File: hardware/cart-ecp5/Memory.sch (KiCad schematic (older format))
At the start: 7 parts, among them J2 MicroSD_Molex_1040310811

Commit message: First pass annotation and footprint assignment complete
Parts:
- gave numbers to parts that had none: 1
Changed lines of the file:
@@
 $EndDescr
 $Comp
-L ng_memory:S27KS0641 U?
+L ng_memory:S27KS0641 U3
 U 1 1 5F47DAAE
 P 3600 4100
-F 0 "U?" H 3900 4900 60  0000 C CNN
+F 0 "U3" H 3900 4900 60  0000 C CNN
 F 1 "S27KS0641" H 4100 4800 60  0000 C CNN
 F 2 "ng_package_bga:BGA-24_6.0x8.0mm_Layout5x5_P1.0mm_Pad0.4mm" H 2800 6050 60  0001 C CNN
@@
 Connection ~ 3500 4850
 $Comp
-L ng_power:GND #PWR?
+L ng_power:GND #PWR09
 U 1 1 5F3CB04C
 P 3500 4950
-F 0 "#PWR?" H 3500 4700 50  0001 C CNN
+F 0 "#PWR09" H 3500 4700 50  0001 C CNN
 F 1 "GND" H 3503 4824 50  0000 C CNN
 F 2 "" H 3400 4600 50  0001 C CNN
@@
 AR Path="/5F8FA3AC" Ref="#PWR?"  Part="1"
 AR Path="/5F8F01DB/5F8FA3AC" Ref="#PWR018"  Part="1"
-AR Path="/5F7B735C/5F8FA3AC" Ref="#PWR?"  Part="1"
-F 0 "#PWR?" H 8400 4650 50  0001 C CNN
+AR Path="/5F7B735C/5F8FA3AC" Ref="#PWR012"  Part="1"
+F 0 "#PWR012" H 8400 4650 50  0001 C CNN
 F 1 "GND" H 8403 4774 50  0000 C CNN
 F 2 "" H 8300 4550 50  0001 C CNN
@@
 AR Path="/5F8FA3B4" Ref="J?"  Part="1"
 AR Path="/5F8F01DB/5F8FA3B4" Ref="J2"  Part="1"
-AR Path="/5F7B735C/5F8FA3B4" Ref="J?"  Part="1"
-F 0 "J?" H 8650 4600 50  0000 L CNN
+AR Path="/5F7B735C/5F8FA3B4" Ref="J2"  Part="1"
+F 0 "J2" H 8650 4600 50  0000 L CNN
 F 1 "MicroSD_Molex_1040310811" H 8650 4500 50  0000 L CNN
 F 2 "ng_conn:MicroSD_Molex_1040310811" H 8700 4000 50  0001 C CNN
@@
 AR Path="/5F8FA3CB" Ref="R?"  Part="1"
 AR Path="/5F8F01DB/5F8FA3CB" Ref="R1"  Part="1"
-AR Path="/5F7B735C/5F8FA3CB" Ref="R?"  Part="1"
-F 0 "R?" V 7700 3300 50  0000 L CNN
+AR Path="/5F7B735C/5F8FA3CB" Ref="R5"  Part="1"
+F 0 "R5" V 7700 3300 50  0000 L CNN
 F 1 "10k" V 7700 3000 50  0000 R CNN
 F 2 "Resistor_SMD:R_0603_1608Metric" V 7580 3150 50  0001 C CNN
@@
 AR Path="/5F8FA3D7" Ref="RN?"  Part="1"
 AR Path="/5F8F01DB/5F8FA3D7" Ref="RN3"  Part="1"
-AR Path="/5F7B735C/5F8FA3D7" Ref="RN?"  Part="1"
-F 0 "RN?" H 8188 3196 50  0000 L CNN
+AR Path="/5F7B735C/5F8FA3D7" Ref="RN1"  Part="1"
+F 0 "RN1" H 8188 3196 50  0000 L CNN
 F 1 "10k" H 8188 3105 50  0000 L CNN
 F 2 "Resistor_SMD:R_Array_Convex_4x0603" V 8275 3150 50  0001 C CNN
@@
 AR Path="/5F8FA3E3" Ref="C?"  Part="1"
 AR Path="/5F8F01DB/5F8FA3E3" Ref="C16"  Part="1"
-AR Path="/5F7B735C/5F8FA3E3" Ref="C?"  Part="1"
-F 0 "C?" H 6850 3150 50  0000 R CNN
+AR Path="/5F7B735C/5F8FA3E3" Ref="C3"  Part="1"
+F 0 "C3" H 6850 3150 50  0000 R CNN
 F 1 "10u" H 6850 2950 50  0000 R CNN
 F 2 "Capacitor_SMD:C_0805_2012Metric" H 6938 2900 50  0001 C CNN
@@
 AR Path="/5F8FA3E9" Ref="C?"  Part="1"
 AR Path="/5F8F01DB/5F8FA3E9" Ref="C17"  Part="1"
-AR Path="/5F7B735C/5F8FA3E9" Ref="C?"  Part="1"
-F 0 "C?" H 7150 3150 50  0000 R CNN
+AR Path="/5F7B735C/5F8FA3E9" Ref="C4"  Part="1"
+F 0 "C4" H 7150 3150 50  0000 R CNN
 F 1 "100n" H 7150 2950 50  0000 R CNN
 F 2 "Capacitor_SMD:C_0603_1608Metric" H 7238 2900 50  0001 C CNN
@@
 AR Path="/5F8FA3EF" Ref="#PWR?"  Part="1"
 AR Path="/5F8F01DB/5F8FA3EF" Ref="#PWR016"  Part="1"
-AR Path="/5F7B735C/5F8FA3EF" Ref="#PWR?"  Part="1"
-F 0 "#PWR?" H 6900 3050 50  0001 C CNN
+AR Path="/5F7B735C/5F8FA3EF" Ref="#PWR010"  Part="1"
+F 0 "#PWR010" H 6900 3050 50  0001 C CNN
 F 1 "GND" H 6903 3174 50  0000 C CNN
 F 2 "" H 6800 2950 50  0001 C CNN
@@
 AR Path="/5F8FA3F5" Ref="#PWR?"  Part="1"
 AR Path="/5F8F01DB/5F8FA3F5" Ref="#PWR017"  Part="1"
-AR Path="/5F7B735C/5F8FA3F5" Ref="#PWR?"  Part="1"
-F 0 "#PWR?" H 7200 3050 50  0001 C CNN
+AR Path="/5F7B735C/5F8FA3F5" Ref="#PWR011"  Part="1"
+F 0 "#PWR011" H 7200 3050 50  0001 C CNN
 F 1 "GND" H 7203 3174 50  0000 C CNN
 F 2 "" H 7100 2950 50  0001 C CNN
@@
 AR Path="/5EFEABF6" Ref="R?"  Part="1"
 AR Path="/5F8F01DB/5EFEABF6" Ref="R8"  Part="1"
-AR Path="/5F7B735C/5EFEABF6" Ref="R?"  Part="1"
-F 0 "R?" V 7600 3300 50  0000 L CNN
+AR Path="/5F7B735C/5EFEABF6" Ref="R4"  Part="1"
+F 0 "R4" V 7600 3300 50  0000 L CNN
 F 1 "10k" V 7600 3000 50  0000 R CNN
 F 2 "Resistor_SMD:R_0603_1608Metric" V 7480 3150 50  0001 C CNN

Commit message: Initial placement pass
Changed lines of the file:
@@
 AR Path="/5F8FA3D7" Ref="RN?"  Part="1"
 AR Path="/5F8F01DB/5F8FA3D7" Ref="RN3"  Part="1"
-AR Path="/5F7B735C/5F8FA3D7" Ref="RN1"  Part="1"
-F 0 "RN1" H 8188 3196 50  0000 L CNN
+AR Path="/5F7B735C/5F8FA3D7" Ref="RN7"  Part="1"
+F 0 "RN7" H 8188 3196 50  0000 L CNN
 F 1 "10k" H 8188 3105 50  0000 L CNN
 F 2 "Resistor_SMD:R_Array_Convex_4x0603" V 8275 3150 50  0001 C CNN

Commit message: Shrink smallest passive to 0402
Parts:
- C16: footprint Capacitor_SMD:C_0805_2012Metric -> Capacitor_SMD:C_0603_1608Metric; MPN CL21A106KAYNNNE -> (none); Place DNP -> (none)
- C17: footprint Capacitor_SMD:C_0603_1608Metric -> Capacitor_SMD:C_0402_1005Metric; MPN CL10B104KB8NNNC -> (none)
- R1, R8: footprint Resistor_SMD:R_0603_1608Metric -> Resistor_SMD:R_0402_1005Metric; MPN RC0603FR-0710KL -> (none)
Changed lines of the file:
@@
 F 0 "R5" V 7700 3300 50  0000 L CNN
 F 1 "10k" V 7700 3000 50  0000 R CNN
-F 2 "Resistor_SMD:R_0603_1608Metric" V 7580 3150 50  0001 C CNN
+F 2 "Resistor_SMD:R_0402_1005Metric" V 7580 3150 50  0001 C CNN
 F 3 "~" H 7650 3150 50  0001 C CNN
-F 4 "RC0603FR-0710KL" H 7650 3150 50  0001 C CNN "MPN"
+F 4 "" H 7650 3150 50  0001 C CNN "MPN"
 	1    7650 3150
 	1    0    0    -1
@@
 F 0 "C3" H 6850 3150 50  0000 R CNN
 F 1 "10u" H 6850 2950 50  0000 R CNN
-F 2 "Capacitor_SMD:C_0805_2012Metric" H 6938 2900 50  0001 C CNN
+F 2 "Capacitor_SMD:C_0603_1608Metric" H 6938 2900 50  0001 C CNN
 F 3 "~" H 6900 3050 50  0001 C CNN
-F 4 "CL21A106KAYNNNE" H 6900 3050 50  0001 C CNN "MPN"
-F 5 "DNP" H 6850 2850 50  0000 R CNN "Place"
+F 4 "" H 6900 3050 50  0001 C CNN "MPN"
 	1    6900 3050
 	-1   0    0    -1
@@
 F 0 "C4" H 7150 3150 50  0000 R CNN
 F 1 "100n" H 7150 2950 50  0000 R CNN
-F 2 "Capacitor_SMD:C_0603_1608Metric" H 7238 2900 50  0001 C CNN
+F 2 "Capacitor_SMD:C_0402_1005Metric" H 7238 2900 50  0001 C CNN
 F 3 "~" H 7200 3050 50  0001 C CNN
-F 4 "CL10B104KB8NNNC" H 7200 3050 50  0001 C CNN "MPN"
+F 4 "" H 7200 3050 50  0001 C CNN "MPN"
 	1    7200 3050
 	-1   0    0    -1
@@
 F 0 "R4" V 7600 3300 50  0000 L CNN
 F 1 "10k" V 7600 3000 50  0000 R CNN
-F 2 "Resistor_SMD:R_0603_1608Metric" V 7480 3150 50  0001 C CNN
+F 2 "Resistor_SMD:R_0402_1005Metric" V 7480 3150 50  0001 C CNN
 F 3 "~" H 7550 3150 50  0001 C CNN
-F 4 "RC0603FR-0710KL" H 7550 3150 50  0001 C CNN "MPN"
+F 4 "" H 7550 3150 50  0001 C CNN "MPN"
 	1    7550 3150
 	1    0    0    -1

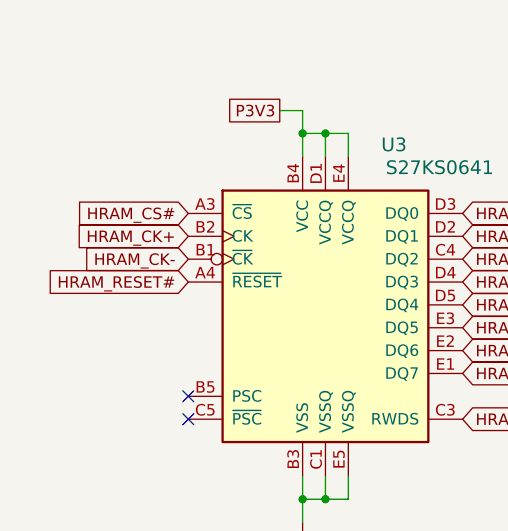
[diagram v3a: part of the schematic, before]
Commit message: Fixes to length matching script, now configured for hyperram
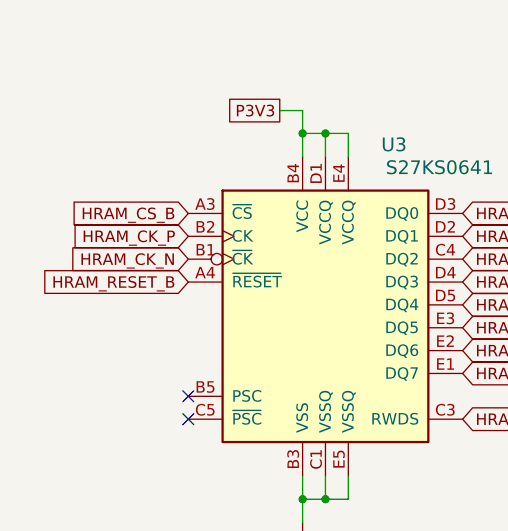
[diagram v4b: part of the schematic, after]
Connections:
- net HRAM_CK+ renamed HRAM_CK_P
- net HRAM_CK- renamed HRAM_CK_N
- net HRAM_CS# renamed HRAM_CS_B
- net HRAM_RESET# renamed HRAM_RESET_B
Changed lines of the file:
@@
 NoConn ~ 3000 4500
 Text GLabel 3000 3600 0    50   Input ~ 0
-HRAM_CS#
+HRAM_CS_B
 Text GLabel 3000 3700 0    50   Input ~ 0
-HRAM_CK+
+HRAM_CK_P
 Text GLabel 3000 3800 0    50   Input ~ 0
-HRAM_CK-
+HRAM_CK_N
 Text GLabel 3000 3900 0    50   Input ~ 0
-HRAM_RESET#
+HRAM_RESET_B
 Wire Wire Line
 	3500 3350 3500 3250

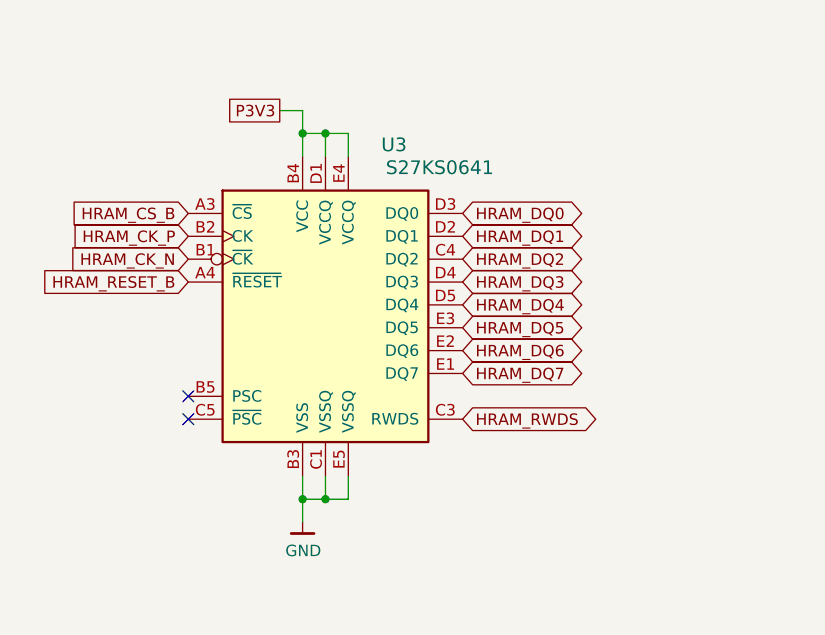
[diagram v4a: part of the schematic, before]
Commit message: Use 1V8 for HyperRAM interface
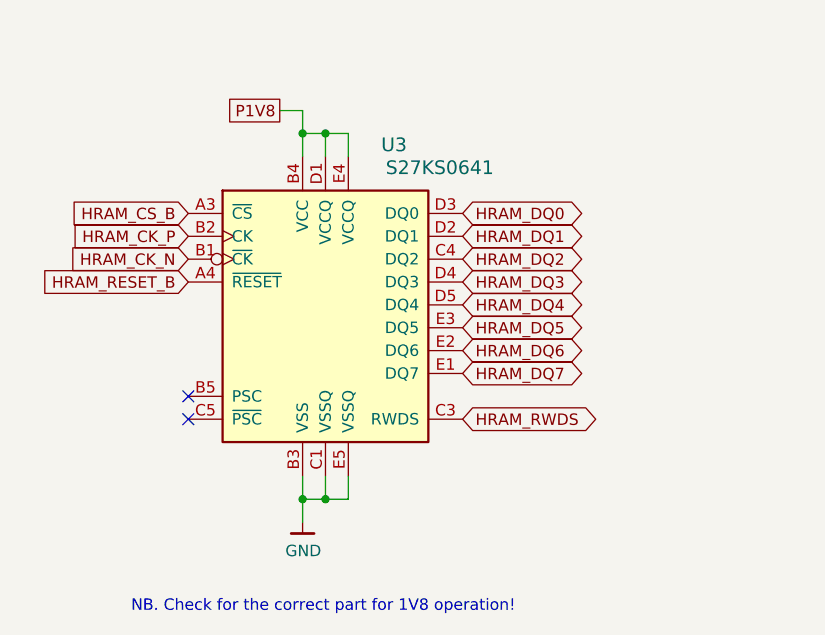
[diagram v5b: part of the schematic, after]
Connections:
- net P3V3: no longer U3.B4 (VCC), U3.D1 (VCCQ), U3.E4 (VCCQ)
- new net P1V8: U3.B4 (VCC), U3.D1 (VCCQ), U3.E4 (VCCQ)
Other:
- note added: "NB. Check for the correct part for 1V8 operation!"
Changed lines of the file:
@@
 Connection ~ 3500 3250
 Text GLabel 3400 3150 0    50   UnSpc ~ 0
-P3V3
+P1V8
 Wire Wire Line
 	3500 4750 3500 4850
@@
 Wire Wire Line
 	8100 3600 8500 3600
+Text Notes 2750 5350 0    50   ~ 0
+NB. Check for the correct part for 1V8 operation!
 $EndSCHEMATC

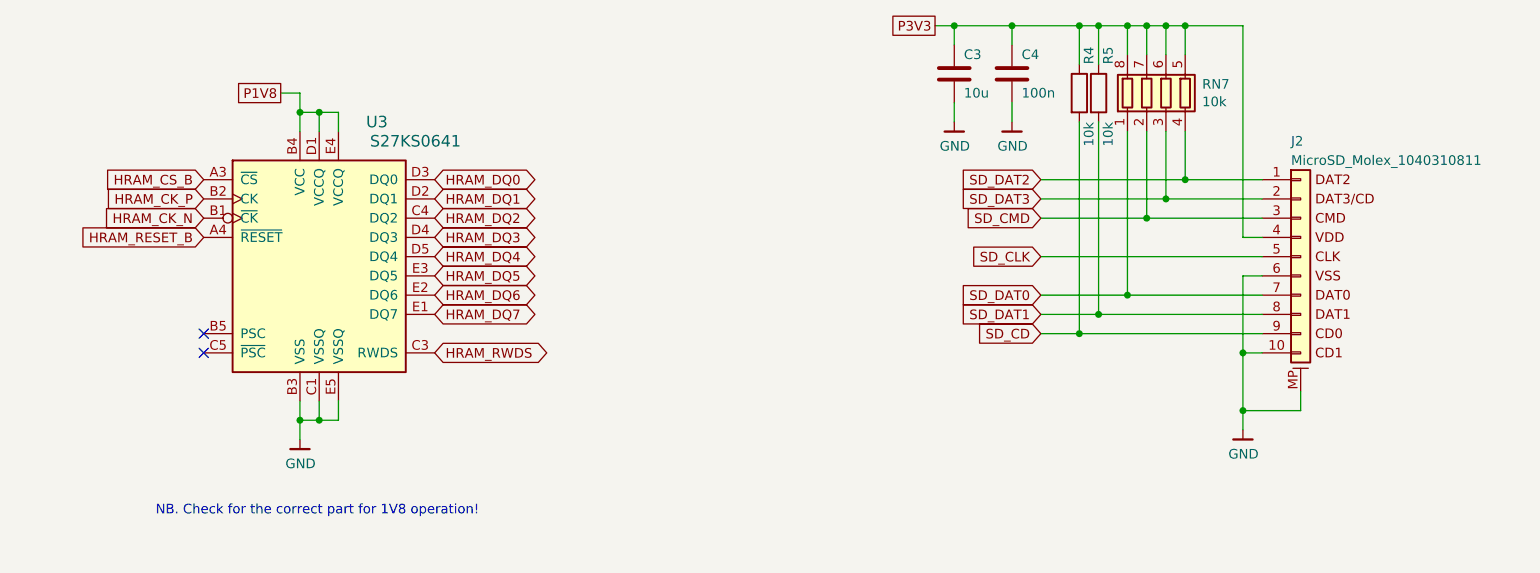
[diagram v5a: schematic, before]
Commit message: Update config flash to WSON package, add HyperRAM decoupling
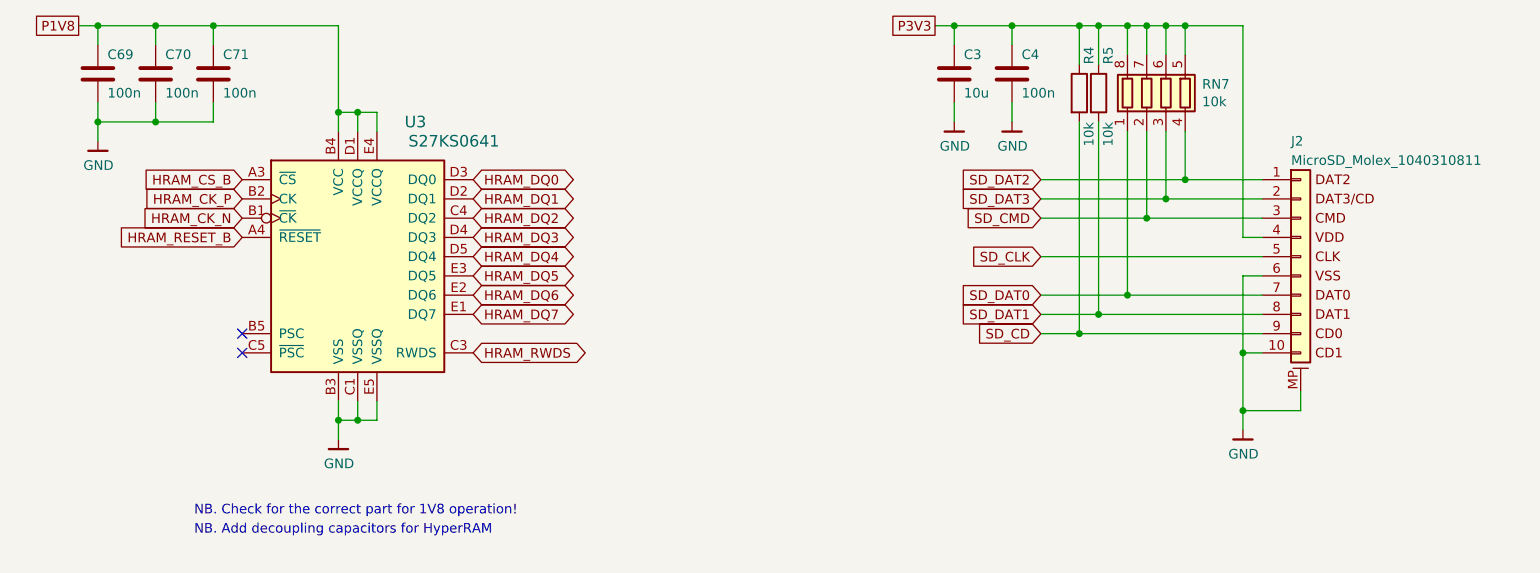
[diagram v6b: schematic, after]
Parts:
- added C69, C70, C71: 100n, Capacitor_SMD:C_0402_1005Metric, symbol Device:C
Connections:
- net GND: now also C69.2, C70.2, C71.2
- net P1V8: now also C69.1, C70.1, C71.1
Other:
- note added: "NB. Add decoupling capacitors for HyperRAM"
- moved on the sheet: U3
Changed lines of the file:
@@
 L ng_memory:S27KS0641 U3
 U 1 1 5F47DAAE
-P 3600 4100
-F 0 "U3" H 3900 4900 60  0000 C CNN
-F 1 "S27KS0641" H 4100 4800 60  0000 C CNN
-F 2 "ng_package_bga:BGA-24_6.0x8.0mm_Layout5x5_P1.0mm_Pad0.4mm" H 2800 6050 60  0001 C CNN
-F 3 "https://www.cypress.com/file/183506/download" H 2800 6050 60  0001 C CNN
-	1    3600 4100
-	1    0    0    -1
-$EndComp
-Text GLabel 4200 3600 2    50   BiDi ~ 0
+P 3800 4100
+F 0 "U3" H 4100 4900 60  0000 C CNN
+F 1 "S27KS0641" H 4300 4800 60  0000 C CNN
+F 2 "ng_package_bga:BGA-24_6.0x8.0mm_Layout5x5_P1.0mm_Pad0.4mm" H 3000 6050 60  0001 C CNN
+F 3 "https://www.cypress.com/file/183506/download" H 3000 6050 60  0001 C CNN
+	1    3800 4100
+	1    0    0    -1
+$EndComp
+Text GLabel 4400 3600 2    50   BiDi ~ 0
 HRAM_DQ0
-Text GLabel 4200 3700 2    50   BiDi ~ 0
+Text GLabel 4400 3700 2    50   BiDi ~ 0
 HRAM_DQ1
-Text GLabel 4200 3800 2    50   BiDi ~ 0
+Text GLabel 4400 3800 2    50   BiDi ~ 0
 HRAM_DQ2
-Text GLabel 4200 3900 2    50   BiDi ~ 0
+Text GLabel 4400 3900 2    50   BiDi ~ 0
 HRAM_DQ3
-Text GLabel 4200 4000 2    50   BiDi ~ 0
+Text GLabel 4400 4000 2    50   BiDi ~ 0
 HRAM_DQ4
-Text GLabel 4200 4100 2    50   BiDi ~ 0
+Text GLabel 4400 4100 2    50   BiDi ~ 0
 HRAM_DQ5
-Text GLabel 4200 4200 2    50   BiDi ~ 0
+Text GLabel 4400 4200 2    50   BiDi ~ 0
 HRAM_DQ6
-Text GLabel 4200 4300 2    50   BiDi ~ 0
+Text GLabel 4400 4300 2    50   BiDi ~ 0
 HRAM_DQ7
-Text GLabel 4200 4500 2    50   BiDi ~ 0
+Text GLabel 4400 4500 2    50   BiDi ~ 0
 HRAM_RWDS
-NoConn ~ 3000 4400
-NoConn ~ 3000 4500
-Text GLabel 3000 3600 0    50   Input ~ 0
+NoConn ~ 3200 4400
+NoConn ~ 3200 4500
+Text GLabel 3200 3600 0    50   Input ~ 0
 HRAM_CS_B
-Text GLabel 3000 3700 0    50   Input ~ 0
+Text GLabel 3200 3700 0    50   Input ~ 0
 HRAM_CK_P
-Text GLabel 3000 3800 0    50   Input ~ 0
+Text GLabel 3200 3800 0    50   Input ~ 0
 HRAM_CK_N
-Text GLabel 3000 3900 0    50   Input ~ 0
+Text GLabel 3200 3900 0    50   Input ~ 0
 HRAM_RESET_B
 Wire Wire Line
-	3500 3350 3500 3250
-Wire Wire Line
-	3500 3250 3600 3250
-Wire Wire Line
-	3700 3250 3700 3350
-Wire Wire Line
-	3600 3350 3600 3250
-Connection ~ 3600 3250
-Wire Wire Line
-	3600 3250 3700 3250
-Wire Wire Line
-	3500 3250 3500 3150
-Wire Wire Line
-	3500 3150 3400 3150
-Connection ~ 3500 3250
-Text GLabel 3400 3150 0    50   UnSpc ~ 0
+	3700 3350 3700 3250
+Wire Wire Line
+	3700 3250 3800 3250
+Wire Wire Line
+	3900 3250 3900 3350
+Wire Wire Line
+	3800 3350 3800 3250
+Connection ~ 3800 3250
+Wire Wire Line
+	3800 3250 3900 3250
+Connection ~ 3700 3250
+Text GLabel 2350 2800 0    50   UnSpc ~ 0
 P1V8
 Wire Wire Line
-	3500 4750 3500 4850
-Wire Wire Line
-	3500 4850 3600 4850
-Wire Wire Line
-	3600 4850 3600 4750
-Wire Wire Line
-	3600 4850 3700 4850
-Wire Wire Line
-	3700 4850 3700 4750
-Connection ~ 3600 4850
-Wire Wire Line
-	3500 4850 3500 4950
-Connection ~ 3500 4850
+	3700 4750 3700 4850
+Wire Wire Line
+	3700 4850 3800 4850
+Wire Wire Line
+	3800 4850 3800 4750
+Wire Wire Line
+	3800 4850 3900 4850
+Wire Wire Line
+	3900 4850 3900 4750
+Connection ~ 3800 4850
+Wire Wire Line
+	3700 4850 3700 4950
+Connection ~ 3700 4850
 $Comp
 L ng_power:GND #PWR09
 U 1 1 5F3CB04C
-P 3500 4950
-F 0 "#PWR09" H 3500 4700 50  0001 C CNN
-F 1 "GND" H 3503 4824 50  0000 C CNN
-F 2 "" H 3400 4600 50  0001 C CNN
-F 3 "" H 3500 4950 50  0001 C CNN
-	1    3500 4950
+P 3700 4950
+F 0 "#PWR09" H 3700 4700 50  0001 C CNN
+F 1 "GND" H 3703 4824 50  0000 C CNN
+F 2 "" H 3600 4600 50  0001 C CNN
+F 3 "" H 3700 4950 50  0001 C CNN
+	1    3700 4950
 	1    0    0    -1
 $EndComp
@@
 Wire Wire Line
 	8100 3600 8500 3600
-Text Notes 2750 5350 0    50   ~ 0
+Text Notes 2950 5350 0    50   ~ 0
 NB. Check for the correct part for 1V8 operation!
+Text Notes 2950 5450 0    50   ~ 0
+NB. Add decoupling capacitors for HyperRAM
+$Comp
+L Device:C C71
+U 1 1 5F5DCC37
+P 3050 3050
+F 0 "C71" H 3100 3150 50  0000 L CNN
+F 1 "100n" H 3100 2950 50  0000 L CNN
+F 2 "Capacitor_SMD:C_0402_1005Metric" H 3088 2900 50  0001 C CNN
+F 3 "~" H 3050 3050 50  0001 C CNN
+	1    3050 3050
+	1    0    0    -1
+$EndComp
+Wire Wire Line
+	3050 3200 3050 3300
+Wire Wire Line
+	3050 2900 3050 2800
+$Comp
+L Device:C C70
+U 1 1 5F5E4A84
+P 2750 3050
+F 0 "C70" H 2800 3150 50  0000 L CNN
+F 1 "100n" H 2800 2950 50  0000 L CNN
+F 2 "Capacitor_SMD:C_0402_1005Metric" H 2788 2900 50  0001 C CNN
+F 3 "~" H 2750 3050 50  0001 C CNN
+	1    2750 3050
+	1    0    0    -1
+$EndComp
+Wire Wire Line
+	2750 3200 2750 3300
+Wire Wire Line
+	2750 2900 2750 2800
+$Comp
+L Device:C C69
+U 1 1 5F5E6253
+P 2450 3050
+F 0 "C69" H 2500 3150 50  0000 L CNN
+F 1 "100n" H 2500 2950 50  0000 L CNN
+F 2 "Capacitor_SMD:C_0402_1005Metric" H 2488 2900 50  0001 C CNN
+F 3 "~" H 2450 3050 50  0001 C CNN
+	1    2450 3050
+	1    0    0    -1
+$EndComp
+Wire Wire Line
+	2450 3200 2450 3300
+Wire Wire Line
+	2450 2900 2450 2800
+Wire Wire Line
+	2450 3300 2750 3300
+Connection ~ 2750 3300
+Wire Wire Line
+	2750 3300 3050 3300
+Wire Wire Line
+	2450 2800 2750 2800
+Wire Wire Line
+	3700 2800 3700 3250
+Connection ~ 2750 2800
+Wire Wire Line
+	2750 2800 3050 2800
+Connection ~ 3050 2800
+Wire Wire Line
+	3050 2800 3700 2800
+Wire Wire Line
+	2450 2800 2350 2800
+Connection ~ 2450 2800
+Wire Wire Line
+	2450 3300 2450 3400
+Connection ~ 2450 3300
+$Comp
+L ng_power:GND #PWR068
+U 1 1 5F5F4633
+P 2450 3400
+F 0 "#PWR068" H 2450 3150 50  0001 C CNN
+F 1 "GND" H 2453 3274 50  0000 C CNN
+F 2 "" H 2350 3050 50  0001 C CNN
+F 3 "" H 2450 3400 50  0001 C CNN
+	1    2450 3400
+	1    0    0    -1
+$EndComp
 $EndSCHEMATC

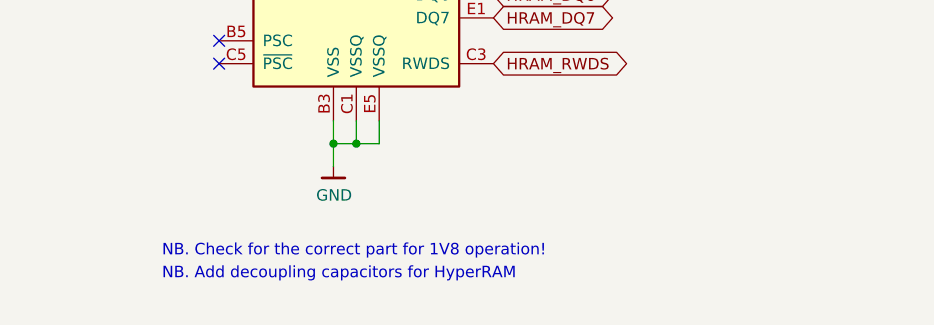
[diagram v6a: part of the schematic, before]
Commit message: Adjust trace widths and spacings for impedance control
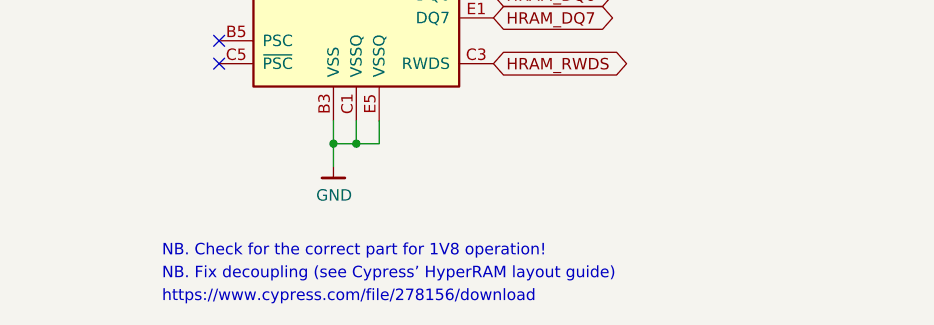
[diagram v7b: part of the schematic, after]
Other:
- note added: "NB. Fix decoupling (see Cypress’ HyperRAM layout guide)"
- note added: "https://www.cypress.com/file/278156/download"
- note removed: "NB. Add decoupling capacitors for HyperRAM"
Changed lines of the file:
@@
 Text Notes 2950 5350 0    50   ~ 0
 NB. Check for the correct part for 1V8 operation!
-Text Notes 2950 5450 0    50   ~ 0
-NB. Add decoupling capacitors for HyperRAM
 $Comp
 L Device:C C71
@@
 	1    0    0    -1
 $EndComp
+Text Notes 2950 5450 0    50   ~ 0
+NB. Fix decoupling (see Cypress’ HyperRAM layout guide)
+Text Notes 2950 5550 0    50   ~ 0
+https://www.cypress.com/file/278156/download
 $EndSCHEMATC
